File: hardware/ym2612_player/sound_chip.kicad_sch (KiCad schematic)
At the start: 28 parts, among them U3 74HCT541, U4 74HCT541, U5 YM2612 (socket only, chip fit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, X1 7.670454 MHz, 5V (not fitted)

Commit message: Mount the Pico Plus 2 on sockets, pick the window LED, tidy labels
The Pico Plus 2 has flash, PSRAM and a connector on its underside, so it
can't be soldered flat. It now plugs into two 1x20 female sockets in the
standard Pico hole pattern; the BOM gains the sockets and the headers for
the module. Tracks around it are re-routed. DRC in KiCad 10: 0 errors,
0 unconnected, matches the schematic.

Window LEDs: Lumimax LED3WAW (3 mm warm white). New tools/silk.py moves
part labels clear of pads and each other; values move to the fab layer.

Co-Authored-By: Claude Opus 5.5 (1M context) <noreply@anthropic.com>
Claude-Session: https://claude.ai/code/session_01JeM5NcWqyQVA3DixJkw6Wg
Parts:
- D1, D2: MPN (none) -> LED3WAW; Spec 3 mm through-hole LED, warm white, about 3V at 5 mA, leads 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 -> 3 mm through-hole LED, warm white 2800K, 3.2V. Any 3 mm war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
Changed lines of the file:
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@@
       (effects (font (size 1.27 1.27)) hide)
     )
-    (property "Spec" "3 mm through-hole LED, warm white, about 3V at 5 mA, leads left long" (at 279.4 111.76 0)
+    (property "MPN" "LED3WAW" (at 279.4 111.76 0)
+      (effects (font (size 1.27 1.27)) hide)
+    )
+    (property "Spec" "3 mm through-hole LED, warm white 2800K, 3.2V. Any 3 mm warm white will do. Leads left long" (at 279.4 111.76 0)
       (effects (font (size 1.27 1.27)) hide)
     )
@@
       (effects (font (size 1.27 1.27)) hide)
     )
-    (property "Spec" "3 mm through-hole LED, warm white, about 3V at 5 mA, leads left long" (at 299.72 111.76 0)
+    (property "MPN" "LED3WAW" (at 299.72 111.76 0)
       (effects (font (size 1.27 1.27)) hide)
     )
+    (property "Spec" "3 mm through-hole LED, warm white 2800K, 3.2V. Any 3 mm warm white will do. Leads left long" (at 299.72 111.76 0)
+      (effects (font (size 1.27 1.27)) hide)
+    )

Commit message: Apply the Rev A fix register: decoupling, single ground, A.VCC filter, TPA6132A2
Schematic
- YM2612 A.VCC (pin 22) gets its own 10 ohm + 220 uF + 100 nF filter.
- /IC, A0, A1 pull-downs 10k -> 4.7k (RP2350 erratum E9).
- Headphone amp: NJM4556A replaced by a TPA6132A2 at -6 dB, no output caps,
  enabled by GP12 (HP_EN, 4.7k pull-down) so power-up doesn't pop.
- 47 uF electrolytic damps the L1/C4 resonance before the LP5907.
- GNDA merged into GND; NT1 removed. Four M3 holes for the LCD standoffs.
- Ferrite label 220R@100MHz to match BLM18PG221SN1D; C15/C22 spec X7R 50V;
  LED lead note for PCBWay.
- Pico Plus 2 and its headers marked do-not-fit (Joey supplies them);
  sockets are Sullins PPTC201LFBN-RC.

Layout
- Decoupling caps placed at the pin they serve (design.NEAR), 2-7 mm instead
  of 16-70 mm.
- One solid GND plane on both layers plus 332 stitching vias (tools/stitch.py).
- J6 moved out from under the LCD backpack; encoder moved below the LCD so
  the knob clears it.
- Re-routed with Freerouting; KiCad 7 DRC: 0 errors, 0 unconnected.

Co-Authored-By: Claude Opus 5.5 (1M context) <noreply@anthropic.com>
Claude-Session: https://claude.ai/code/session_01T6y8roX1LzS9uTuKVQBe9X
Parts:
- removed R5, R6: 100, Resistor_SMD:R_0603_1608Metric, symbol Device:R
- removed U3: 74HCT541, Package_SO:SOIC-20W_7.5x12.8mm_P1.27mm, symbol 74xx:74HCT541
- added C13, C16: 100nF, Capacitor_SMD:C_0603_1608Metric, symbol Device:C
- added C14: 10uF, Capacitor_SMD:C_0805_2012Metric, symbol Device:C
- added C15: 220uF, Capacitor_SMD:CP_Elec_6.3x7.7, symbol Device:C_Polarized
- added R21: 10, Resistor_SMD:R_0603_1608Metric, symbol Device:R
- C12: renamed from C14; value 10uF -> 100nF; footprint Capacitor_SMD:C_0805_2012Metric -> Capacitor_SMD:C_0603_1608Metric; Spec X5R, 16V, 0805 -> X7R, 16V
- D1: renamed from C9; value 100nF -> warm white 3 mm; footprint Capacitor_SMD:C_0603_1608Metric -> LED_THT:LED_D3.0mm; symbol Device:C -> Device:LED; MPN (none) -> LED3WAW; Spec X7R, 16V -> 3 mm through-hole LED, warm white 2800K, 3.2V. Any 3 mm war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
- D2: renamed from C11; value 100nF -> warm white 3 mm; footprint Capacitor_SMD:C_0603_1608Metric -> LED_THT:LED_D3.0mm; symbol Device:C -> Device:LED; MPN (none) -> LED3WAW; Spec X7R, 16V -> 3 mm through-hole LED, warm white 2800K, 3.2V. Any 3 mm war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
- R10: renamed from U4; value 74HCT541 -> 100; footprint Package_SO:SOIC-20W_7.5x12.8mm_P1.27mm -> Resistor_SMD:R_0603_1608Metric; symbol 74xx:74HCT541 -> Device:R; MPN 74HCT541D,653 -> (none); Spec octal buffer, HCT, SOIC-20 -> 1%, 0603
- R14: renamed from R17; value 33 -> 100
- R15: renamed from R18; value 33 -> 100; now fitted
- R16: renamed from X1; value 7.670454 MHz, 5V (not fitted) -> 100; footprint Oscillator:Oscillator_DIP-8 -> Resistor_SMD:R_0603_1608Metric; symbol Oscillator:CXO_DIP8 -> Device:R; Spec half-size DIP-8 oscillator can, 5V CMOS, 7.670454 MHz -> 1%, 0603; now fitted
- R17: renamed from U5; value YM2612 (socket only, chip fitted by hand) -> 33; footprint Package_DIP:DIP-24_W15.24mm_Socket -> Resistor_SMD:R_0603_1608Metric; symbol ym2612:YM2612 -> Device:R; MPN 110-43-624-41-001000 -> (none); Spec Mill-Max 24-pin 600 mil turned-pin DIP socket. PCBWay fits 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 -> 1%, 0603
- R18: renamed from R19; value 430 -> 33; now not fitted
- R19: renamed from D2; value warm white 3 mm -> 430; footprint LED_THT:LED_D3.0mm -> Resistor_SMD:R_0603_1608Metric; symbol Device:LED -> Device:R; MPN LED3WAW -> (none); Spec 3 mm through-hole LED, warm white 2800K, 3.2V. Any 3 mm war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 -> 1%, 0603
- R20: renamed from C10; value 100nF -> 430; footprint Capacitor_SMD:C_0603_1608Metric -> Resistor_SMD:R_0603_1608Metric; symbol Device:C -> Device:R; Spec X7R, 16V -> 1%, 0603
- U3: renamed from R7; value 100 -> 74HCT541; footprint Resistor_SMD:R_0603_1608Metric -> Package_SO:SOIC-20W_7.5x12.8mm_P1.27mm; symbol Device:R -> 74xx:74HCT541; MPN (none) -> 74HCT541D,653; Spec 1%, 0603 -> octal buffer, HCT, SOIC-20
- U4: renamed from R15; value 100 -> 74HCT541; footprint Resistor_SMD:R_0603_1608Metric -> Package_SO:SOIC-20W_7.5x12.8mm_P1.27mm; symbol Device:R -> 74xx:74HCT541; MPN (none) -> 74HCT541D,653; Spec 1%, 0603 -> octal buffer, HCT, SOIC-20
- U5: renamed from R20; value 430 -> YM2612 (socket only, chip fitted by hand); footprint Resistor_SMD:R_0603_1608Metric -> Package_DIP:DIP-24_W15.24mm_Socket; symbol Device:R -> ym2612:YM2612; MPN (none) -> 110-43-624-41-001000; Spec 1%, 0603 -> Mill-Max 24-pin 600 mil turned-pin DIP socket. PCBWay fits 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
- X1: renamed from D1; value warm white 3 mm -> 7.670454 MHz, 5V (not fitted); footprint LED_THT:LED_D3.0mm -> Oscillator:Oscillator_DIP-8; symbol Device:LED -> Oscillator:CXO_DIP8; MPN LED3WAW -> (none); Spec 3 mm through-hole LED, warm white 2800K, 3.2V. Any 3 mm war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 -> half-size DIP-8 oscillator can, 5V CMOS, 7.670454 MHz; now not fitted
- renumbered C12 to C10, C13 to C11, R13 to R11, R14 to R12, R16 to R13, R8 to R5, R9 to R6, R10 to R7, R11 to R8, R12 to R9
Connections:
- net +5V: now also R19.1, R20.1; no longer R18.1, U5.1
- net +5V_YM: now also U3.20 (VCC), U4.20 (VCC), U5.16 (~{RD}), U5.23 (VCC), X1.1 (EN), X1.8 (Vcc), C13.1, C14.1, R21.1; no longer D1.1, D2.1, R10.20 (VCC), R16.1 (EN), R16.8 (Vcc), R17.16 (~{RD}), R17.22 (A.VCC), R17.23 (VCC), R20.1
- net GND: now also D1.1 (K), D2.1 (K), U3.1 (G1), U3.10 (GND), U3.19 (G2), U4.1 (G1), U4.10 (GND), U4.19 (G2), U4.7 (A5), U4.8 (A6), U4.9 (A7), U5.1 (GND), U5.12 (GND), U5.14 (~{CS}), U5.19 (A.GND), X1.4 (GND), C13.2, C14.2, C15.2, C16.2; no longer D1.2, D2.2, R10.1 (G1), R10.10 (GND), R10.19 (G2), R10.7 (A5), R10.8 (A6), R10.9 (A7), R16.4 (GND), R17.1 (GND), R17.12 (GND), R17.14 (~{CS}), R19.1 (K), R20.2, X1.1 (K)
- net LED_WIN1: now also D1.2 (A), R19.2; no longer R18.2, X1.2 (A)
- net LED_WIN2: now also D2.2 (A), R20.2; no longer R19.2 (A), U5.2
- net MCU_A0: now also U4.2 (A0); no longer R10.2 (A0)
- net MCU_A1: now also U4.3 (A1); no longer R10.3 (A1)
- net MCU_CLK: now also U4.6 (A4); no longer R10.6 (A4)
- net MCU_D0: now also U3.2 (A0)
- net MCU_D1: now also U3.3 (A1)
- net MCU_D2: now also U3.4 (A2)
- net MCU_D3: now also U3.5 (A3)
- net MCU_D4: now also U3.6 (A4)
- net MCU_D5: now also U3.7 (A5)
- net MCU_D6: now also U3.8 (A6)
- net MCU_D7: now also U3.9 (A7)
- net MCU_IC: now also U4.5 (A3); no longer R10.5 (A3)
- net MCU_WR: now also U4.4 (A2); no longer R10.4 (A2)
- net OSC_OUT: now also R18.1, X1.5 (OUT); no longer R15.1, R16.5 (OUT)
- net YMB_A0: now also R13.1, U4.18 (Y0); no longer R10.18 (Y0), R11.1
- net YMB_A1: now also R14.1, U4.17 (Y1); no longer R10.17 (Y1), R12.1
- net YMB_CLK: now also R17.1, U4.14 (Y4); no longer R10.14 (Y4), R14.1
- net YMB_D0: now also R5.1, U3.18 (Y0)
- net YMB_D1: now also R6.1, U3.17 (Y1)
- net YMB_D2: now also R7.1, U3.16 (Y2); no longer U3.1
- net YMB_D3: now also R8.1, U3.15 (Y3); no longer R5.1
- net YMB_D4: now also R9.1, U3.14 (Y4); no longer R6.1
- net YMB_D5: now also R10.1, U3.13 (Y5); no longer R7.1
- net YMB_D6: now also R11.1, U3.12 (Y6); no longer R8.1
- net YMB_D7: now also R12.1, U3.11 (Y7); no longer R9.1
- net YMB_IC: now also R16.1, U4.15 (Y3); no longer R10.15 (Y3), R13.1
- net YMB_WR: now also R15.1, U4.16 (Y2); no longer R10.16 (Y2), U4.1
- net YM_A0: now also R13.2, U5.17 (A0); no longer R11.2, R17.17 (A0)
- net YM_A1: now also R14.2, U5.18 (A1); no longer R12.2, R17.18 (A1)
- net YM_CLK: now also R17.2, R18.2, U5.24 (ΦM); no longer R14.2, R15.2, R17.24 (ΦM)
- net YM_D0: now also R5.2, U5.2 (D0); no longer R17.2 (D0)
- net YM_D1: now also R6.2, U5.3 (D1); no longer R17.3 (D1)
- net YM_D2: now also R7.2, U5.4 (D2); no longer R17.4 (D2), U3.2
- net YM_D3: now also R8.2, U5.5 (D3); no longer R17.5 (D3), R5.2
- net YM_D4: now also R9.2, U5.6 (D4); no longer R17.6 (D4), R6.2
- net YM_D5: now also R10.2, U5.7 (D5); no longer R17.7 (D5), R7.2
- net YM_D6: now also R11.2, U5.8 (D6); no longer R17.8 (D6), R8.2
- net YM_D7: now also R12.2, U5.9 (D7); no longer R17.9 (D7), R9.2
- net YM_IC: now also R16.2, U5.11 (~{IC}); no longer R13.2, R17.11 (~{IC})
- net YM_MOL: now also U5.20 (MOL); no longer R17.20 (MOL)
- net YM_MOR: now also U5.21 (MOR); no longer R17.21 (MOR)
- net YM_WR: now also R15.2, U5.15 (~{WR}); no longer R17.15 (~{WR}), U4.2
- removed net GNDA: R17.19 (A.GND)
- new net YM_AVCC: C15.1, C16.1, R21.2, U5.22 (A.VCC)
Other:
- note added: "Decoupling: one 100nF at each 74HCT541, one at YM2612 VCC (pin 23) with 10uF bulk, one for X1. A.VCC (pin 22): 10 ohm + 220uF + 100nF filter, placed at pins 22 and 19."
- note removed: "Decoupling: one 100nF at each 74HCT541, two at the YM2612 (VCC pin 23, A.VCC pin 22), one for X1, plus 10uF bulk at the YM2612."
- moved on the sheet: C10, C11, C12, R11, R12, R13, R14, R5, R6, R7, R8, R9

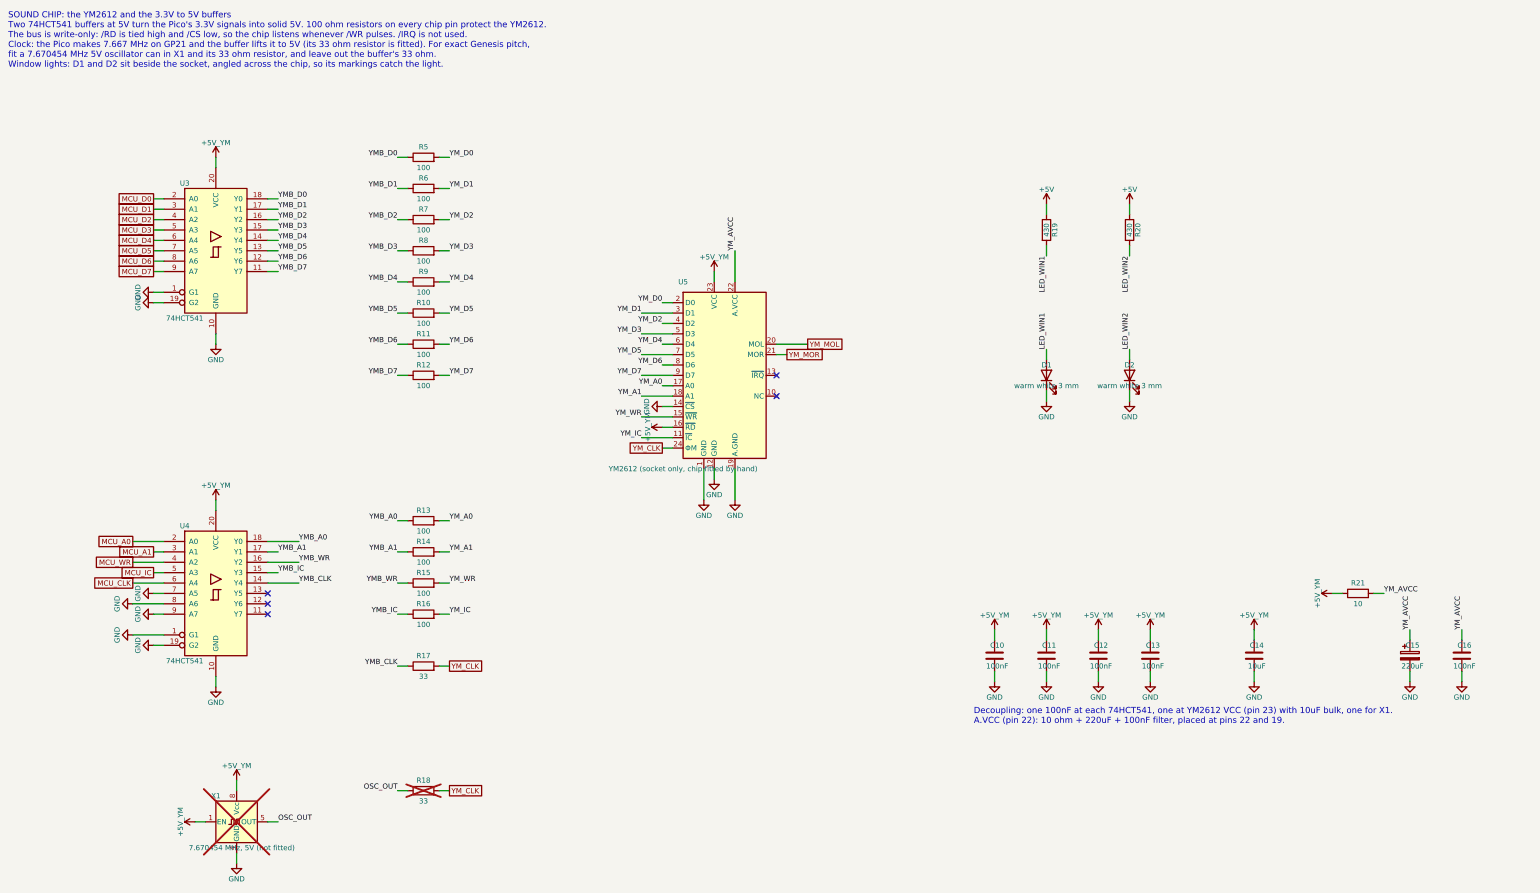
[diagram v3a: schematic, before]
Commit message: Schematic: draw real wires between parts instead of name tags
tools/wires.py routes each page's nets on the 1.27 mm grid around part bodies and text.
Power pins keep power symbols (neighbouring pins share one), signals that leave a page get
one global label, and the netlist check still matches design.py exactly (0 mismatches).
Sound chip and audio pages re-laid out so the wiring reads left to right; title blocks say Rev B.

Co-Authored-By: Claude Opus 5.5 <noreply@anthropic.com>
Claude-Session: https://claude.ai/code/session_01TDTDVidYRoyJdUGgsyVTSw
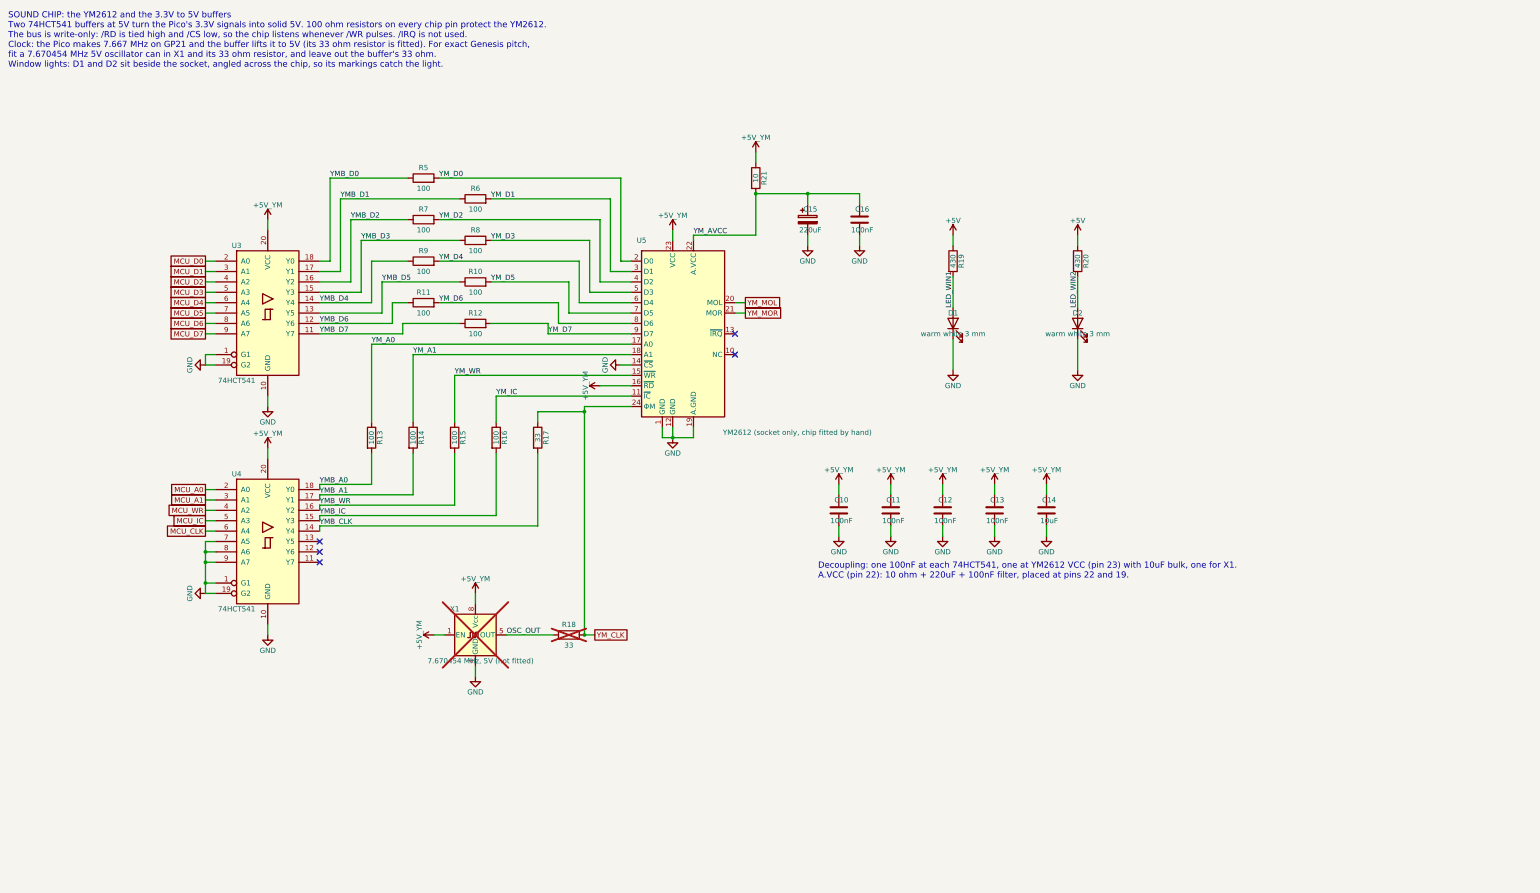
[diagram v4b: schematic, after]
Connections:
- net OSC_OUT: now also R18.2; no longer R18.1
- net YMB_A0: now also R13.2; no longer R13.1
- net YMB_A1: now also R14.2; no longer R14.1
- net YMB_CLK: now also R17.2; no longer R17.1
- net YMB_IC: now also R16.2; no longer R16.1
- net YMB_WR: now also R15.2; no longer R15.1
- net YM_A0: now also R13.1; no longer R13.2
- net YM_A1: now also R14.1; no longer R14.2
- net YM_CLK: now also R17.1, R18.1; no longer R17.2, R18.2
- net YM_IC: now also R16.1; no longer R16.2
- net YM_WR: now also R15.1; no longer R15.2
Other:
- moved on the sheet: C10, C11, C12, C13, C14, C15, C16, D1, D2, R10, R11, R12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

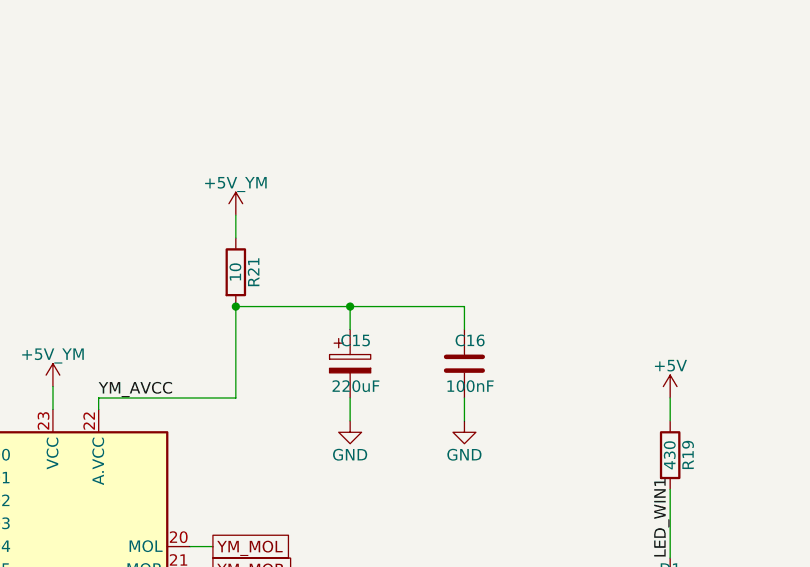
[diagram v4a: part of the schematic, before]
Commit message: Schematic: PWR_FLAG on YM_AVCC (KiCad 10 ERC: A.VCC is fed through R21)
Co-Authored-By: Claude Opus 5.5 <noreply@anthropic.com>
Claude-Session: https://claude.ai/code/session_01TDTDVidYRoyJdUGgsyVTSw
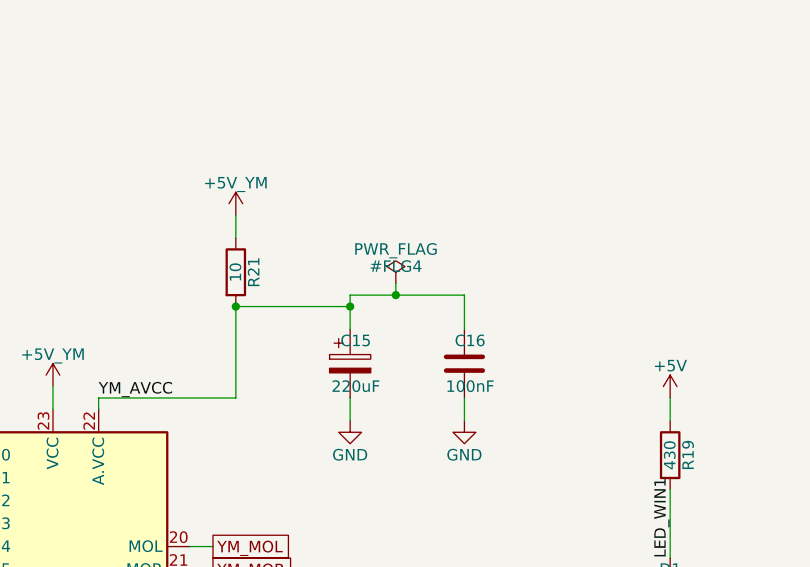
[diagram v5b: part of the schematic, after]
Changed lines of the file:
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@@
+    )
+  )
+  (symbol (lib_id "power:PWR_FLAG") (at 226.06 64.77 0) (unit 1)
+    (in_bom yes) (on_board yes) (dnp no)
+    (property "Reference" "#FLG4" (at 226.06 62.865 0)
+      (effects (font (size 1.27 1.27)))
+    )
+    (property "Value" "PWR_FLAG" (at 226.06 60.96 0)
+      (effects (font (size 1.27 1.27)))
+    )
+    (property "Footprint" "" (at 226.06 64.77 0)
+      (effects (font (size 1.27 1.27)) hide)
+    )
+    (property "Datasheet" "" (at 226.06 64.77 0)
+      (effects (font (size 1.27 1.27)) hide)
+    )
+    (pin "1")
+    (instances
+      (project "ym2612_player"
+        (path "/41b11b85-050a-5903-b32f-6fc3659dbce6/fd13e24a-73fe-5ba1-a493-4b705efd2e66"
+          (reference "#FLG4") (unit 1)
+        )
+      )
     )
   )
@@
     (effects (font (size 1.27 1.27)) (justify left bottom))
   )
-  (wire (pts (xy 220.98 67.31) (xy 233.68 67.31))
+  (wire (pts (xy 220.98 67.31) (xy 220.98 66.04))
     (stroke (width 0) (type default))
   )
@@
     (stroke (width 0) (type default))
   )
+  (wire (pts (xy 226.06 66.04) (xy 233.68 66.04))
+    (stroke (width 0) (type default))
+  )
+  (wire (pts (xy 226.06 66.04) (xy 220.98 66.04))
+    (stroke (width 0) (type default))
+  )
+  (wire (pts (xy 226.06 66.04) (xy 226.06 64.77))
+    (stroke (width 0) (type default))
+  )
   (wire (pts (xy 193.04 78.74) (xy 193.04 77.47))
     (stroke (width 0) (type default))
   )
-  (wire (pts (xy 233.68 67.31) (xy 233.68 69.85))
-    (stroke (width 0) (type default))
-  )
   (wire (pts (xy 193.04 77.47) (xy 208.28 77.47))
     (stroke (width 0) (type default))
   )
+  (wire (pts (xy 233.68 69.85) (xy 233.68 66.04))
+    (stroke (width 0) (type default))
+  )
   (label "YM_AVCC" (at 193.04 77.47 0) (fields_autoplaced)
     (effects (font (size 1.27 1.27)) (justify left bottom))
@@
   (junction (at 220.98 67.31) (diameter 0) (color 0 0 0 0)
   )
+  (junction (at 226.06 66.04) (diameter 0) (color 0 0 0 0)
+  )
   (junction (at 208.28 67.31) (diameter 0) (color 0 0 0 0)
